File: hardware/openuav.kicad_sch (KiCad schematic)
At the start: 85 parts, among them J1 Conn_01x01, J10 Conn_01x01, J11 Conn_01x01, J12 Conn_01x01, J13 Conn_01x01, J14 Conn_01x01, J15 Conn_01x01, J16 Conn_01x01, J17 Conn_01x01, J18 Conn_01x01, J19 Conn_01x01, J2 Conn_01x01, J20 Conn_01x01, J21 Conn_01x01, J22 Conn_01x01, J23 Conn_01x01, J24 Conn_01x01, J25 Conn_01x01, J3 Conn_01x01, J4 Conn_01x01, J5 Conn_01x01, J6 Conn_01x01, J7 Conn_01x01, J8 Conn_01x01, J9 Conn_01x01, J99 USB_C_Receptacle_USB2.0, SW1 SW_Push, SW2 SW_Push, U1 STM32G431CBUx, U2 LPS22HH, U3 LSM6DSR, U4 SY8303, U5 SY8303, U6 W25N01GVZEIG, U7 TLV75733PDBV

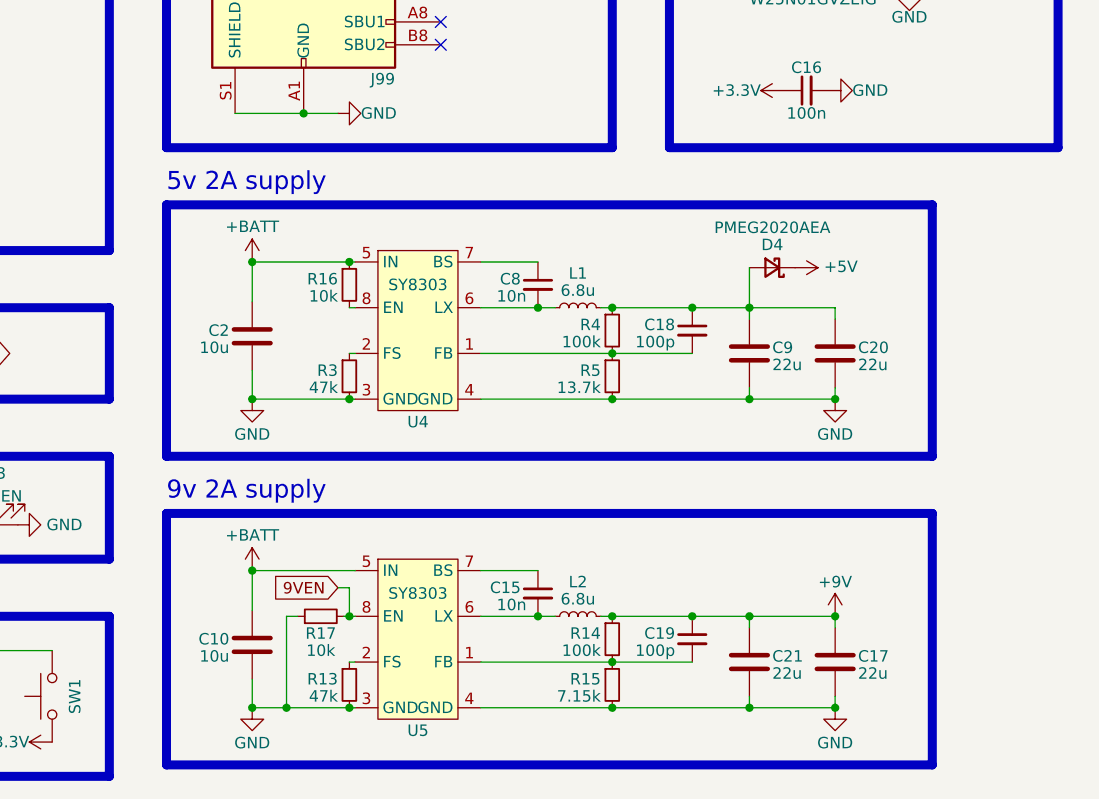
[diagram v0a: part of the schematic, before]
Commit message: Remove SMPS in preparation for next attempt
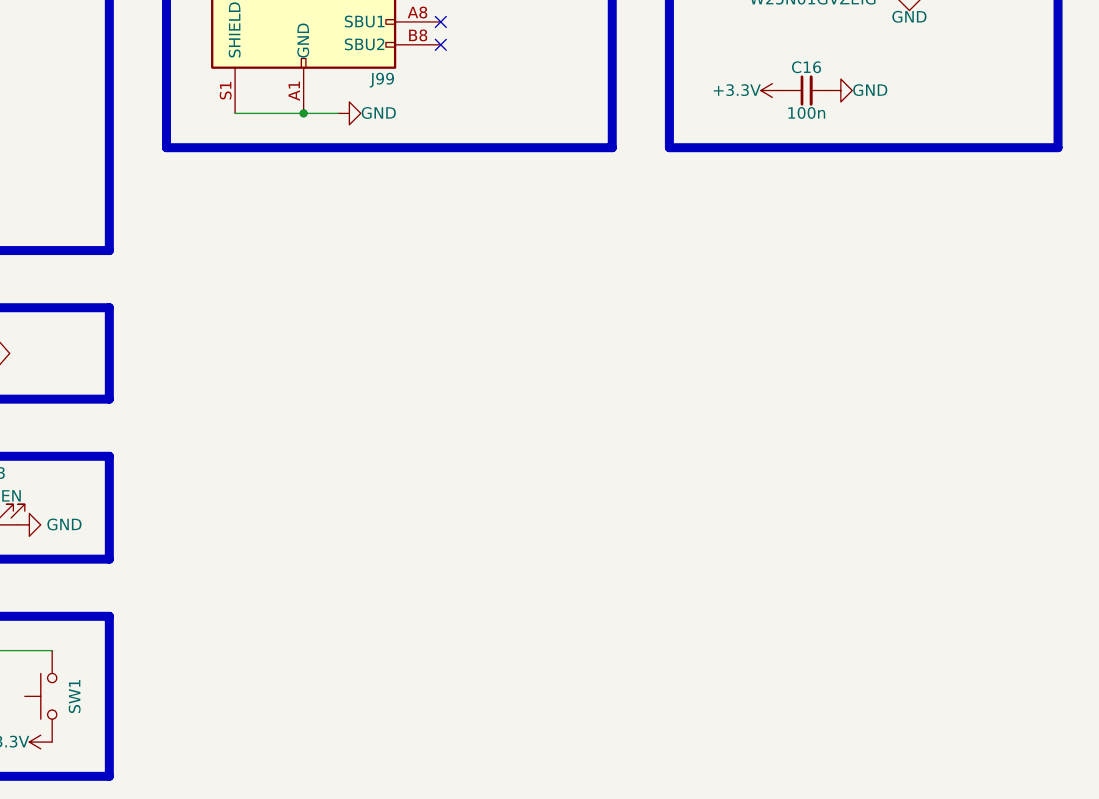
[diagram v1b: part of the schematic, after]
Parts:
- removed C10, C2: 10u, Capacitor_SMD:C_1206_3216Metric, symbol Device:C
- removed C15, C8: 10n, Capacitor_SMD:C_0402_1005Metric, symbol Device:C_Small
- removed C17, C20, C21, C9: 22u, Capacitor_SMD:C_0805_2012Metric, symbol Device:C
- removed C18, C19: 100p, Capacitor_SMD:C_0402_1005Metric, symbol Device:C_Small
- removed D4: PMEG2020AEA, Diode_SMD:D_SOD-323, symbol Device:D_Schottky_Small
- removed L1, L2: 6.8u, Inductor_SMD:L_Sunlord_MWSA0402S, symbol Device:L_Small
- removed R13, R3: 47k, Resistor_SMD:R_0402_1005Metric, symbol Device:R_Small
- removed R14, R4: 100k, Resistor_SMD:R_0402_1005Metric, symbol Device:R_Small
- removed R15: 7.15k, Resistor_SMD:R_0402_1005Metric, symbol Device:R_Small
- removed R16, R17: 10k, Resistor_SMD:R_0402_1005Metric, symbol Device:R_Small
- removed R5: 13.7k, Resistor_SMD:R_0402_1005Metric, symbol Device:R_Small
- removed U4, U5: SY8303, Package_TO_SOT_SMD:TSOT-23-8, symbol openuav:SY8303
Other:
- note removed: "5v 2A supply"
- note removed: "9v 2A supply"

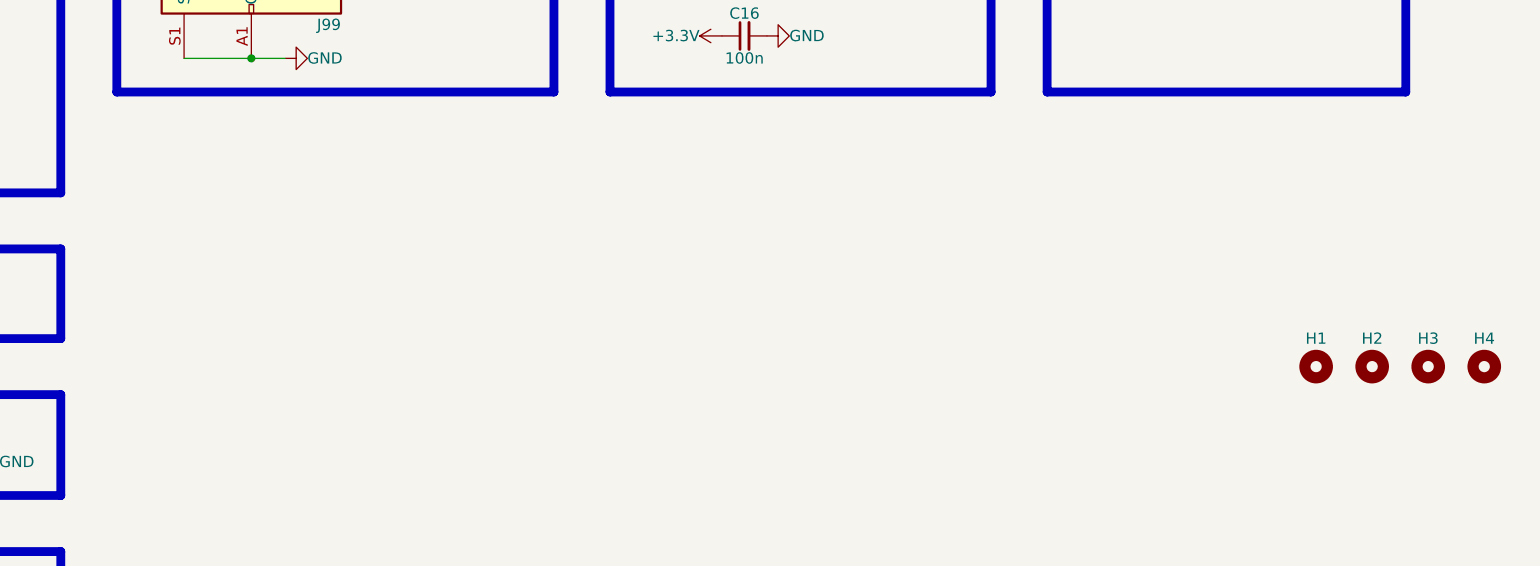
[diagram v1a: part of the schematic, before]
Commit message: Begin TI SMPS design
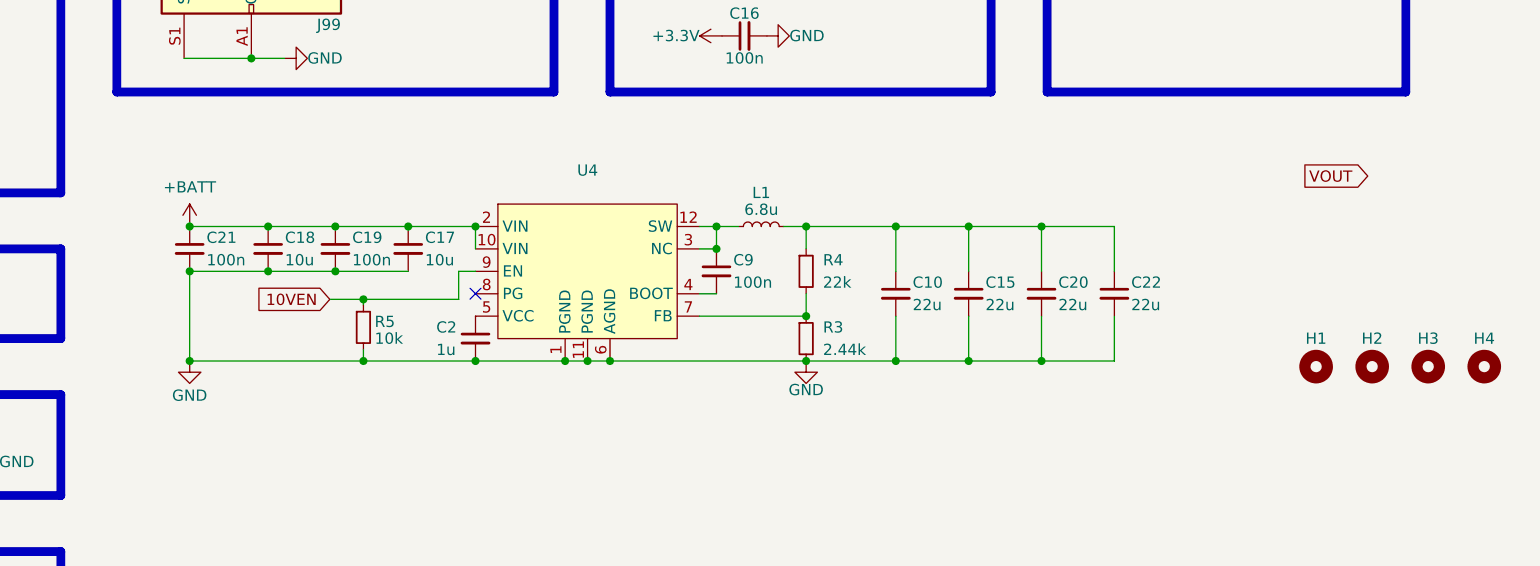
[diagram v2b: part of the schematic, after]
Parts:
- added C10, C15, C20, C22: 22u, Capacitor_SMD:C_0805_2012Metric, symbol Device:C_Small
- added C17, C18: 10u, Capacitor_SMD:C_0805_2012Metric, symbol Device:C_Small
- added C19, C21, C9: 100n, Capacitor_SMD:C_0402_1005Metric, symbol Device:C_Small
- added C2: 1u, Capacitor_SMD:C_0402_1005Metric, symbol Device:C_Small
- added L1: 6.8u, Inductor_SMD:L_Sunlord_MWSA0503S, symbol Device:L_Small
- added R3: 2.44k, Resistor_SMD:R_0402_1005Metric, symbol Device:R_Small
- added R4: 22k, Resistor_SMD:R_0402_1005Metric, symbol Device:R_Small
- added R5: 10k, Resistor_SMD:R_0402_1005Metric, symbol Device:R_Small
- added U4: ~, footprints:RNX0012B, symbol openuav:LMR33630BRNXR
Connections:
- net +BATT: now also C17.1, C18.1, C19.1, C21.1, U4.10 (VIN), U4.2 (VIN)
- net GND: now also C10.2, C15.2, C17.2, C18.2, C19.2, C2.2, C20.2, C21.2, C22.2, R3.2, R5.2, U4.1 (PGND), U4.11 (PGND), U4.6 (AGND)
- new net: C10.1, C15.1, C20.1, C22.1, L1.2, R4.1
- new net: C9.1, L1.1, U4.12 (SW), U4.3 (NC)
- new net: C9.2, U4.4 (BOOT)
- new net: R3.1, R4.2, U4.7 (FB)
- new net: C2.1, U4.5 (VCC)
- new net 10VEN: R5.1, U4.9 (EN)
- no-connect marks 10 -> 11

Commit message: Work in progress new SMPS
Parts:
- removed R5: 10k, Resistor_SMD:R_0402_1005Metric, symbol Device:R_Small
- removed SW2: SW_Push, Button_Switch_SMD:SW_SPST_B3U-1000P, symbol Switch:SW_Push
- added C23: 10u, Capacitor_SMD:C_1206_3216Metric, symbol Device:C_Small
- added C26, C30: 1u, Capacitor_SMD:C_0402_1005Metric, symbol Device:C_Small
- added C27, C8: 100n, Capacitor_SMD:C_0402_1005Metric, symbol Device:C_Small
- added C28, C29: 22u, Capacitor_SMD:C_1206_3216Metric, symbol Device:C_Small
- added C31, C32: 1u, Capacitor_SMD:C_0402_1005Metric, symbol Device:C
- added C33, C34, C35: 10u, Capacitor_SMD:C_0603_1608Metric, symbol Device:C
- added D4: PMEG2020AEA, Diode_SMD:D_SOD-323, symbol Device:D_Schottky_Small
- added FB1: FerriteBead, Inductor_SMD:L_0805_2012Metric, symbol Device:FerriteBead
- added L2: 10u, Inductor_SMD:L_Sunlord_MWSA0503S, symbol Device:L_Small
- added R13: 10k, Resistor_SMD:R_0402_1005Metric, symbol Device:R_Small
- added R14: 22k, Resistor_SMD:R_0402_1005Metric, symbol Device:R_Small
- added R15: 2.44k, Resistor_SMD:R_0402_1005Metric, symbol Device:R_Small
- added U5: ~, footprints:RNX0012B, symbol openuav:LMR33630BRNXR
- added U8: TLV75733PDBV, Package_TO_SOT_SMD:SOT-23-5, symbol Regulator_Linear:TLV75733PDBV
- C10, C15: footprint Capacitor_SMD:C_0805_2012Metric -> Capacitor_SMD:C_1206_3216Metric; LCSC C45783 -> C12891
- C17, C18: footprint Capacitor_SMD:C_0805_2012Metric -> Capacitor_SMD:C_1206_3216Metric; LCSC C440198 -> C13585
- C20: value 22u -> 10u; footprint Capacitor_SMD:C_0805_2012Metric -> Capacitor_SMD:C_1206_3216Metric; LCSC C45783 -> C13585
- C22: value 22u -> 100n; footprint Capacitor_SMD:C_0805_2012Metric -> Capacitor_SMD:C_0402_1005Metric; LCSC C45783 -> C1525
- J15, J16: footprint footprints:smallpad -> footprints:largepad
- L1: value 6.8u -> 10u; LCSC C408411 -> (none)
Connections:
- net 10VEN is gone; now on net 9VEN: U4.9 (EN)
- net +3V3: now also C34.1; no longer C3.1, U3.8 (Vdd)
- net +5V: now also C31.1, C33.1, C35.1, D4.1 (K), U8.1 (IN), U8.3 (EN)
- net +9V: now also C10.1, C15.1, L1.2, R4.1
- net +BATT: now also C20.1, C22.1, C23.1, C8.1, U5.10 (VIN), U5.2 (VIN)
- net 9VEN: now also R13.1
- net GND: now also C23.2, C26.2, C28.2, C29.2, C30.2, C31.2, C32.2, C33.2, C34.2, C35.2, C8.2, R13.2, R15.2, U5.1 (PGND), U5.11 (PGND), U5.6 (AGND), U8.2 (GND)
- new net: C28.1, C29.1, D4.2 (A), L2.2, R14.1
- new net: C32.1, FB1.1, U8.5 (OUT)
- new net: R14.2, R15.1, U5.7 (FB)
- new net: C27.1, L2.1, U5.12 (SW), U5.3 (NC)
- new net: C27.2, U5.4 (BOOT)
- new net: C26.1, U5.5 (VCC)
- new net VDDA: C3.1, C30.1, FB1.2, U3.8 (Vdd)
- no-connect marks 11 -> 12
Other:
- note added: "5V 2A Supply"
- note added: "9V 2A Supply"
- note added: "Gyro Analog Supply"
- note added: "Reset circuit"
- note removed: "Reset switch"
- moved on the sheet: C10, C11, C15, C17, C18, C19, C2, C21, C3, C9, H1, H2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
